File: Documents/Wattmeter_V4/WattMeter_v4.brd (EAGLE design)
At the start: 64.5 x 35.5 mm, 88 parts, among them Q1 QUARTZ_3.58M_2PIN, U1 ADE7953, U10 PS2505, U11 SN74LVC1G3157DBVR, U12 PS2505, U13 SN74LVC, U2 PAM2305, U3 ISO7241, U4 SN74LVC, U5 NL17SZ125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

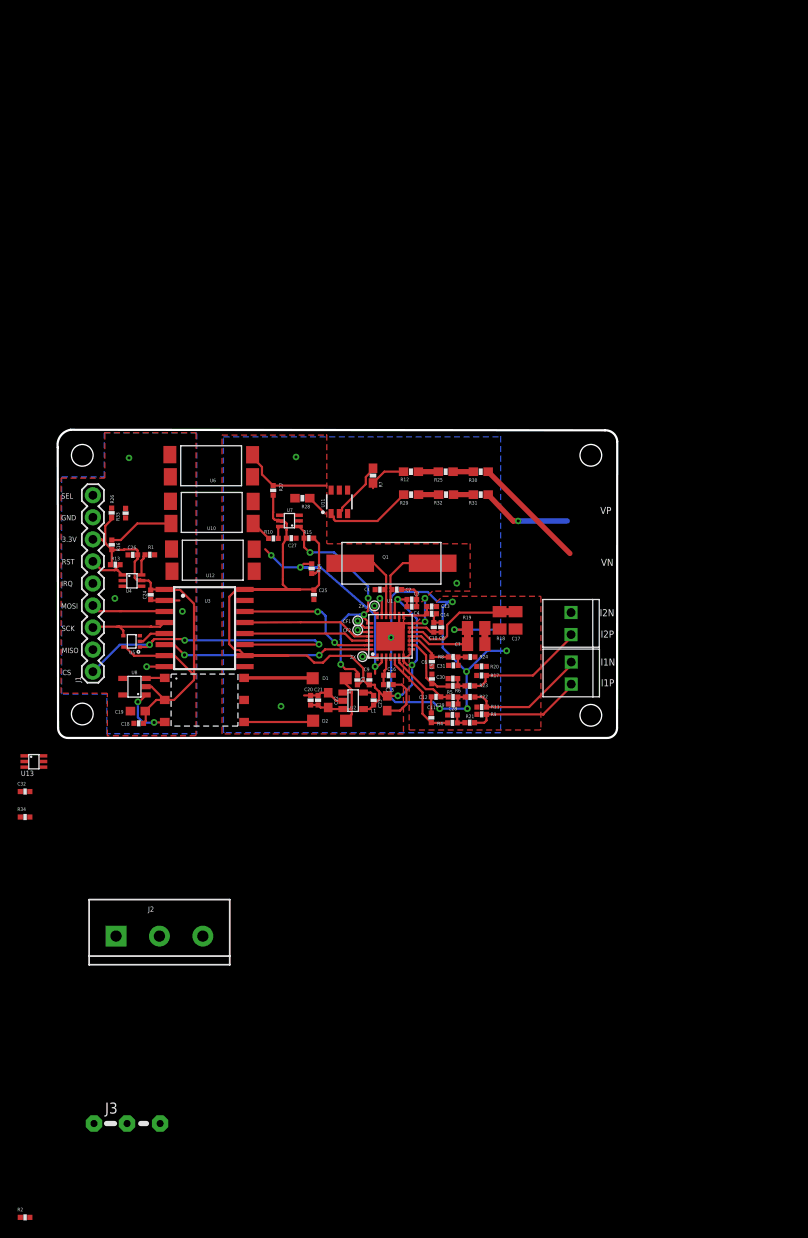
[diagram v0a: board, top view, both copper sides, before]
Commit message: latest updates for I2C and SPI
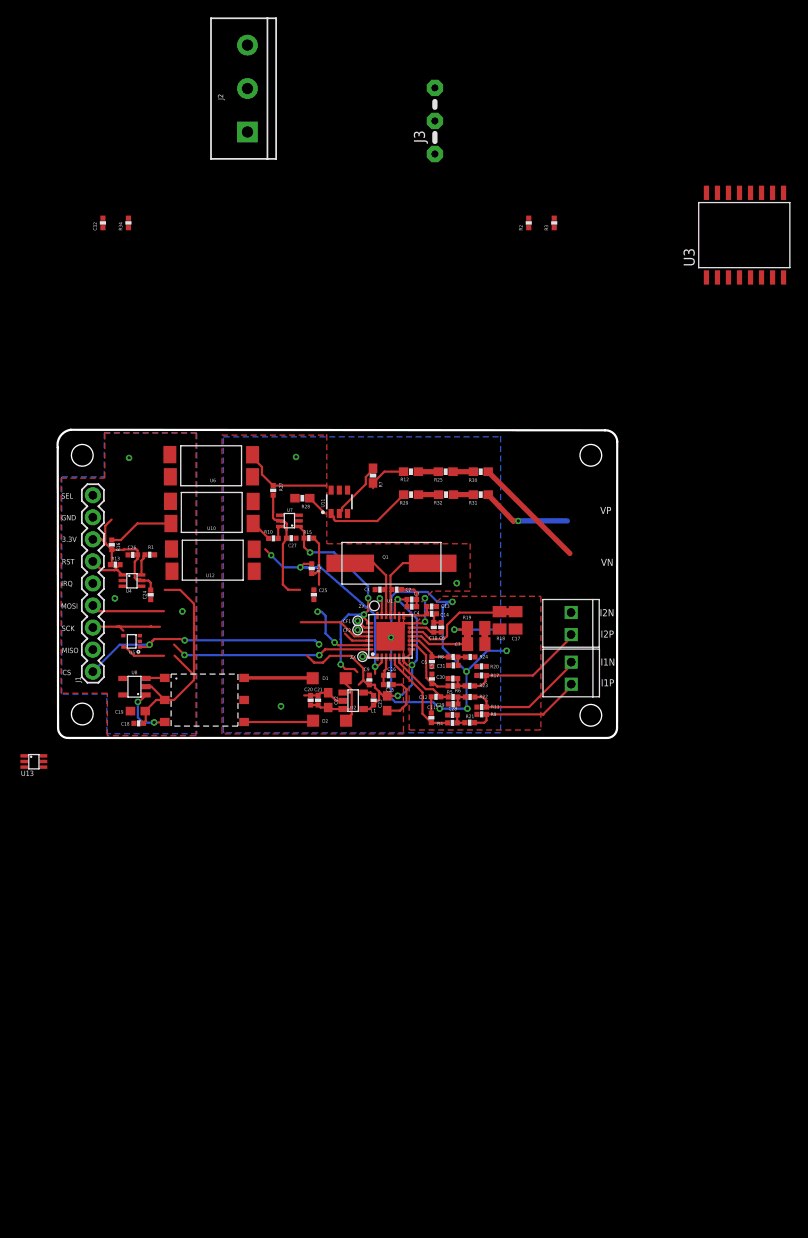
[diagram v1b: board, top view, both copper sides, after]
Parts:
- removed R26, R33: 4.7k, Nizanlib:0402-RES
- R3: value 10k -> 4.7k
- U3: device Damien_divers:16-SOIC -> wattmeter:16-SOIC
- moved R2 128.4 mm to (54.5, 59.7), turned to 90 degrees
- moved J3 119.6 mm to (43.7, 69.5), turned to 90 degrees
- moved J2 93.9 mm to (22.1, 70.1), turned to 90 degrees
- moved U3 84.3 mm to (83.9, 53.4), turned to 90 degrees
- moved R34 69.5 mm to (8.43, 59.7), turned to 90 degrees
- moved C32 66.1 mm to (5.50, 59.7), turned to 90 degrees
- moved R3 57.3 mm to (57.5, 59.7)
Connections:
- net IRQ renamed IRQ_OUT
- removed net +3V3: U11.5
- removed net N$29: U11.6, U7.4
- net GND: now also R3.1; no longer R33.1
- net IRQ_ISO: no longer R3.2
- net MISO_OUT: now also U5.4
- net N$40: now also R3.2
- net N$42: no longer R26.1, R33.2
- net SCK: no longer U3.4, U5.4
- net SETPHASE: now also U11.6; no longer U7.3
- net VCC: now also U11.5; no longer R3.1
- net VDD: no longer R26.2
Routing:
- net VCC: track 96.6 -> 59.0 mm
- net MISO_ISO: track 15.1 -> 3.60 mm
- net CS: track 37.7 -> 29.2 mm
- net MOSI_ISO: track 17.2 -> 8.81 mm
- net SCK_ISO: track 15.0 -> 8.61 mm
- net GND: track 5.78 -> 0.53 mm, vias 4 -> 3
- net MISO: track 3.19 -> 0.00 mm
- net VDD: track 52.7 -> 49.6 mm
- net SCK: track 10.1 -> 8.88 mm
- net ZX_I: track 1.25 -> 0.00 mm, vias 1 -> 0
- net CS_ISO: track 24.4 -> 23.3 mm
